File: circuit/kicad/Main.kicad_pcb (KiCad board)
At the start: 2 copper layers, 110.8 x 117 mm, 104 parts, among them J1 SH3, J10 PA3, J11 SH4, J2 SH3, J3 FFC6, J4 SH6, J5 FTSH2x5, J6 FFC4, J7 SH4, J8 FFC12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

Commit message: パーツ配置まではとりあえず終わらせた。後は配線すればいい。
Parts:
- moved C19 11.3 mm to (-18.0, 2.80), turned to 0 degrees
- moved C21 9.73 mm to (-19.5, -6.20), turned to 270 degrees
- moved FB3 9.35 mm to (-22.0, -6.20), turned to 90 degrees
- moved FB2 6.09 mm to (-22.0, 2.80), turned to 0 degrees
- moved J10 2.50 mm to (-22.0, -1.50), turned to 180 degrees
- moved D10 0.90 mm to (-25.5, -10.0)
- moved R20 0.90 mm to (-21.5, -10.0)
- moved R21 0.75 mm to (-23.5, -11.5)
- renumbered D to D6, D to D9
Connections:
- J8 pad 6: /Rotary1 -> /Rotary4
- J8 pad 8: /Rotary4 -> /Rotary8
- J8 pad 9: /Rotary8 -> /Rotary1

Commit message: hoge
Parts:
- J8: footprint Connector_PinHeader_1.00mm:PinHeader_1x12_P1.00mm_Vertical -> FFC:WürthElektronik_687112183722_01x12_P0.5mm
- U3: footprint ICM-20648:QFN40P300X300X95-24N -> Package_DFN_QFN:QFN-24-1EP_3x3mm_P0.4mm_EP1.75x1.6mm
- moved C15 18.4 mm to (-1.30, 4.40), turned to 270 degrees
- moved C11 17.5 mm to (3.70, -11.8)
- moved D11 15.0 mm to (25.5, 12.0), turned to 0 degrees
- moved BZ1 9.92 mm to (25.5, 17.4), turned to 0 degrees
- moved Q10 9.53 mm to (17.9, 17.4)
- moved R32 9.48 mm to (14.2, 16.6), turned to 0 degrees
- moved R33 8.96 mm to (14.2, 18.1)
- moved J8 5.46 mm to (14.6, 36.8), turned to 0 degrees
- moved RN1 4.74 mm to (-7.10, -8.20), turned to 90 degrees
- moved C10 4.10 mm to (27.8, -0.50)
- moved U1 4.10 mm to (25.8, -0.50)
- moved D3 2.29 mm to (-24.4, -51.3), turned to 26.2 degrees
- moved D13 2.18 mm to (24.4, -51.4), turned to 153.7 degrees
- moved D2 2.12 mm to (-30.8, -47.7), turned to 33.7 degrees
- moved D8 2.09 mm to (10.3, -55.9), turned to 168.7 degrees
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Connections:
- U2 pad 10: Net-(J3-Pad4) -> /Sensor10
- U2 pad 11: Net-(J3-Pad5) -> /Sensor09
- U2 pad 14: /Sensor12 -> /Sensor08
- U2 pad 15: /Sensor11 -> /Sensor07
- U2 pad 16: /Sensor10 -> Net-(J3-Pad2)
- U2 pad 17: /Sensor09 -> Net-(J3-Pad3)
- U2 pad 20: /Sensor08 -> Net-(J3-Pad4)
- U2 pad 21: /Sensor07 -> Net-(J3-Pad5)
- U2 pad 34: /Rotary8 -> /LED_Red
- U2 pad 39: /LED_Red -> /LED_White
- U2 pad 40: /LED_White -> /LED_B
- U2 pad 43: /Rotary4 -> /LED_G
- U2 pad 44: /Rotary2 -> /LED_R
- U2 pad 45: /Rotary1 -> /Rotary4
- U2 pad 51: /LED_B -> /Rotary2
- U2 pad 52: /LED_G -> /Rotary8
- U2 pad 53: /LED_R -> /Rotary1
- U2 pad 8: Net-(J3-Pad2) -> /Sensor12
- U2 pad 9: Net-(J3-Pad3) -> /Sensor11
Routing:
- net +3V3: track 0.00 -> 442.2 mm, vias 0 -> 22
- net +5V: track 0.00 -> 130.5 mm, vias 0 -> 6
- net nRST: track 0.00 -> 108.0 mm
- net /LED_Red: track 0.00 -> 95.9 mm, vias 0 -> 4
- net USART_TX: track 0.00 -> 94.9 mm, vias 0 -> 2
- net USART_RX: track 0.00 -> 91.7 mm, vias 0 -> 2
- net /LED_White: track 0.00 -> 81.2 mm, vias 0 -> 4
- net /LED_B: track 0.00 -> 78.6 mm, vias 0 -> 4
- net /LED_G: track 0.00 -> 74.6 mm, vias 0 -> 4
- net ICM_nCS: track 0.00 -> 66.9 mm, vias 0 -> 4
- net SWO: track 0.00 -> 63.0 mm, vias 0 -> 4
- net Encorder1_A: track 0.00 -> 54.2 mm, vias 0 -> 2
- net /SW3: track 0.00 -> 53.5 mm
- net SWCLK: track 0.00 -> 53.2 mm
- net SWDIO: track 0.00 -> 53.0 mm, vias 0 -> 2
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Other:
- net class Default: clearance 0.2 -> 0.19
- rule trace_clearance: 0.2 -> 0.19
- rule trace_min: 0.2 -> 0.1524
- rule via_min_size: 0.4 -> 0.1524

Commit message: とりあえず完成
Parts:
- turned Q8 to 348.7 degrees
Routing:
- net /Sensor12: track 25.7 -> 94.6 mm
- net /Sensor11: track 24.6 -> 88.8 mm
- net /Sensor10: track 23.7 -> 83.4 mm
- net /Sensor09: track 23.5 -> 80.4 mm
- net /Sensor01: track 28.4 -> 83.1 mm, vias 2 -> 4
- net /Sensor02: track 29.2 -> 81.4 mm, vias 2 -> 3
- net /Sensor03: track 28.2 -> 74.8 mm, vias 2 -> 3
- net /Sensor04: track 26.9 -> 67.2 mm, vias 2 -> 3
- net /Sensor05: track 26.8 -> 64.2 mm, vias 2 -> 3
- net /Sensor06: track 26.2 -> 59.7 mm, vias 2 -> 3
- net /Sensor07: track 32.3 -> 63.8 mm, vias 2 -> 3
- net /Sensor08: track 32.5 -> 62.7 mm, vias 2 -> 1
- net +3V3: track 442.2 -> 469.3 mm
- net Net-(J3-Pad2): track 29.2 -> 47.9 mm, vias 1 -> 0
- net Net-(J3-Pad3): track 28.7 -> 47.2 mm, vias 1 -> 0
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- added copper zone on F.Cu, net GND

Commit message: 点検
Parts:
- moved C5 1.00 mm to (21.2, 3.25), turned to 270 degrees
- moved C6 1.00 mm to (19.7, 3.25), turned to 270 degrees
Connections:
- J1 pad MP: (no net) -> GND
- J11 pad MP: (no net) -> GND
- J2 pad MP: (no net) -> GND
- J3 pad MP: (no net) -> GND
- J4 pad MP: (no net) -> GND
- J6 pad MP: (no net) -> GND
- J7 pad MP: (no net) -> GND
- J8 pad MP: (no net) -> GND
- U3 pad 25: (no net) -> GND
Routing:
- net GND: track 5.36 -> 38.7 mm, vias 0 -> 157
- net +5V: track 130.5 -> 143.0 mm
- net +3V3: track 469.3 -> 465.7 mm, vias 22 -> 20
- net /Rotary1: track 44.4 -> 41.0 mm
- net /Rotary8: track 44.9 -> 41.9 mm
- net /Rotary2: track 44.1 -> 41.2 mm
- net /Sensor08: track 62.7 -> 65.4 mm, vias 1 -> 2
- net USART_RX: track 91.7 -> 93.3 mm
- net USART_TX: track 94.3 -> 95.9 mm
- net /SW3: track 53.5 -> 54.2 mm
- net nRST: track 108.0 -> 108.8 mm
- added copper zone on B.Cu, net GND

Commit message: hoge
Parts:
- moved J10 0.10 mm to (-22.0, -1.40)
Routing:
- net I2C_SCL: track 46.0 -> 43.4 mm
- net I2C_SDA: track 44.9 -> 43.6 mm
- net GND: vias 157 -> 159

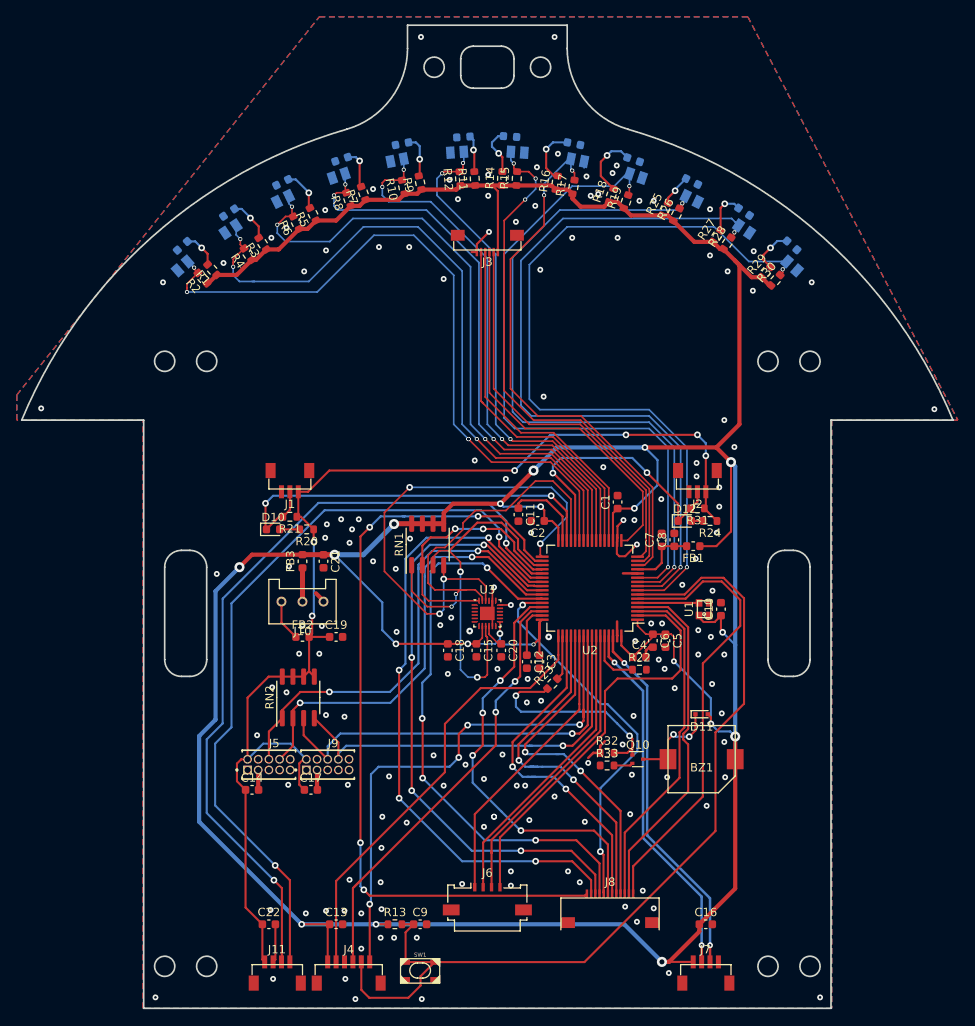
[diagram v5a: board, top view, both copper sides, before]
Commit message: あとはシルクを見やすい位置にもっていくだけ。
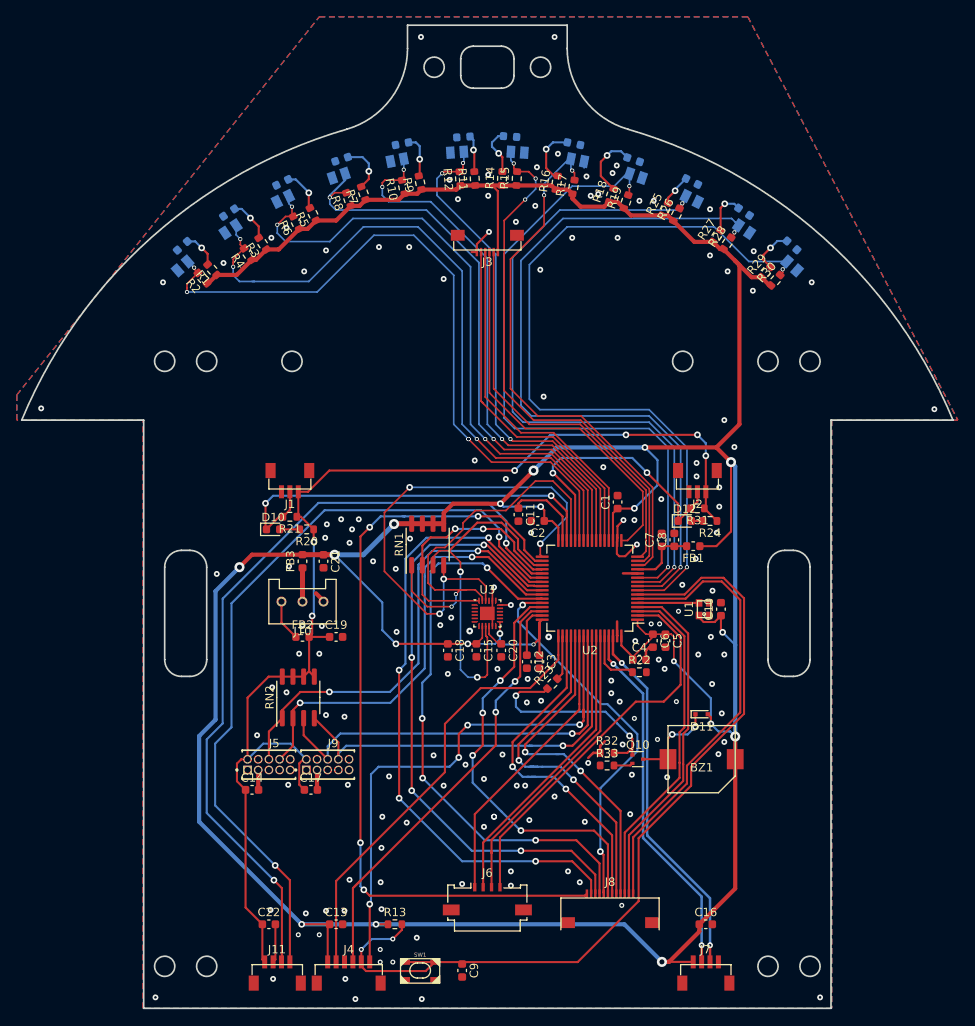
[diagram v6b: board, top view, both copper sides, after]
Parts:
- moved C9 7.43 mm to (-3.00, 42.5), turned to 270 degrees
- moved C4 0.30 mm to (18.1, 5.50)
- moved R22 0.30 mm to (18.1, 7.00)
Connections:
- J1 pad MP: GND -> (no net)
- J2 pad MP: GND -> (no net)
- J3 pad MP: GND -> (no net)
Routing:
- net nRST: track 108.8 -> 105.2 mm, vias 0 -> 2
- net /DRV2_EN: track 49.1 -> 46.8 mm
- net /Sensor04: track 67.2 -> 69.4 mm, vias 3 -> 2
- net Net-(D4-Pad2): track 4.74 -> 5.96 mm
- net GND: track 38.7 -> 37.6 mm, vias 159 -> 157
- net /SW2: track 42.1 -> 41.2 mm
- net /SW1: track 40.9 -> 40.4 mm
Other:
- outline, holes or cut-outs redrawn
- rule trace_min: 0.1524 -> 0.2
